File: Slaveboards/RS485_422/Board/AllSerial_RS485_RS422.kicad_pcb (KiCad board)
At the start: 2 copper layers, 67.4 x 44.8 mm, 18 parts, among them IC1 7402D, IC2 MAX485CSA, IC3 MAX485CSA, IC4 MAX485CSA, IC5 MAX485CSA, J1 PinHeader_2x05_P2.54mm_Horizo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, X1 ALLSERIALSLAVE, X2 AKL18X-10W

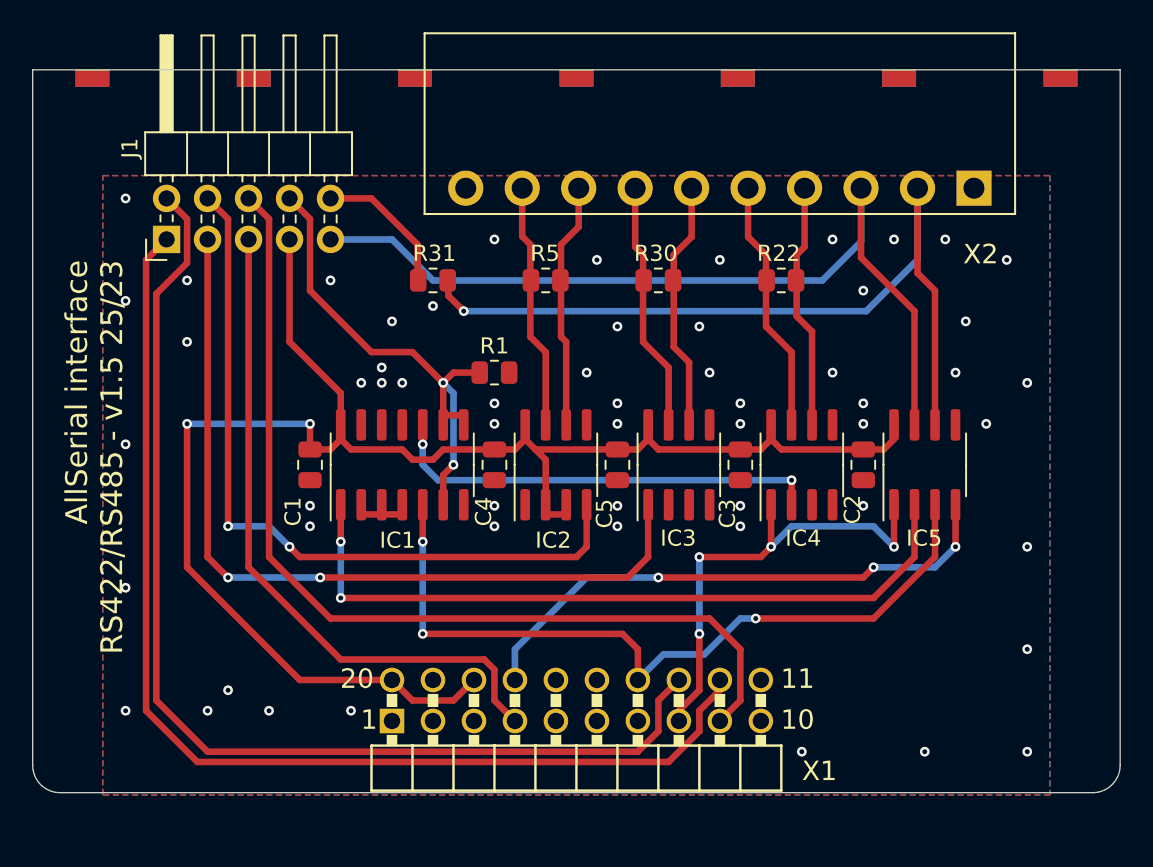
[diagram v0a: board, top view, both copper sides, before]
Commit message: Update AllSerial libraries
update projects
add slave project template
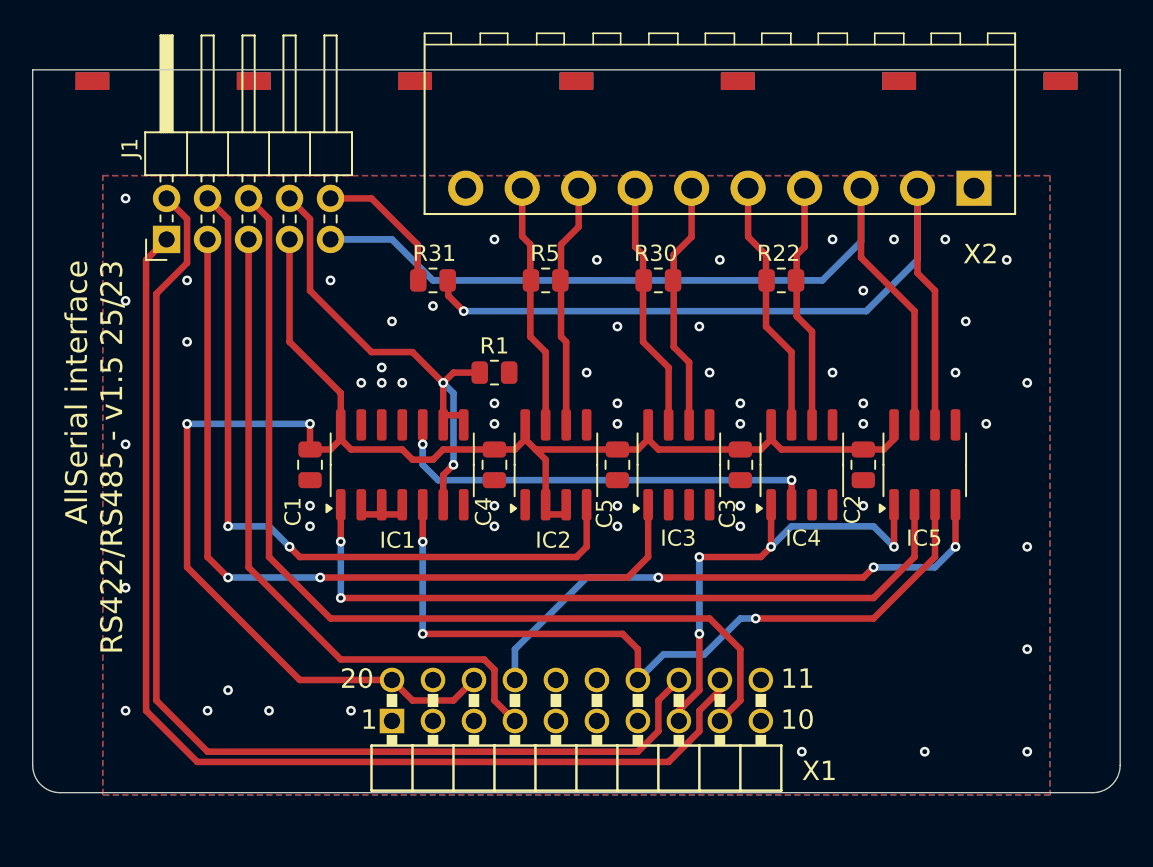
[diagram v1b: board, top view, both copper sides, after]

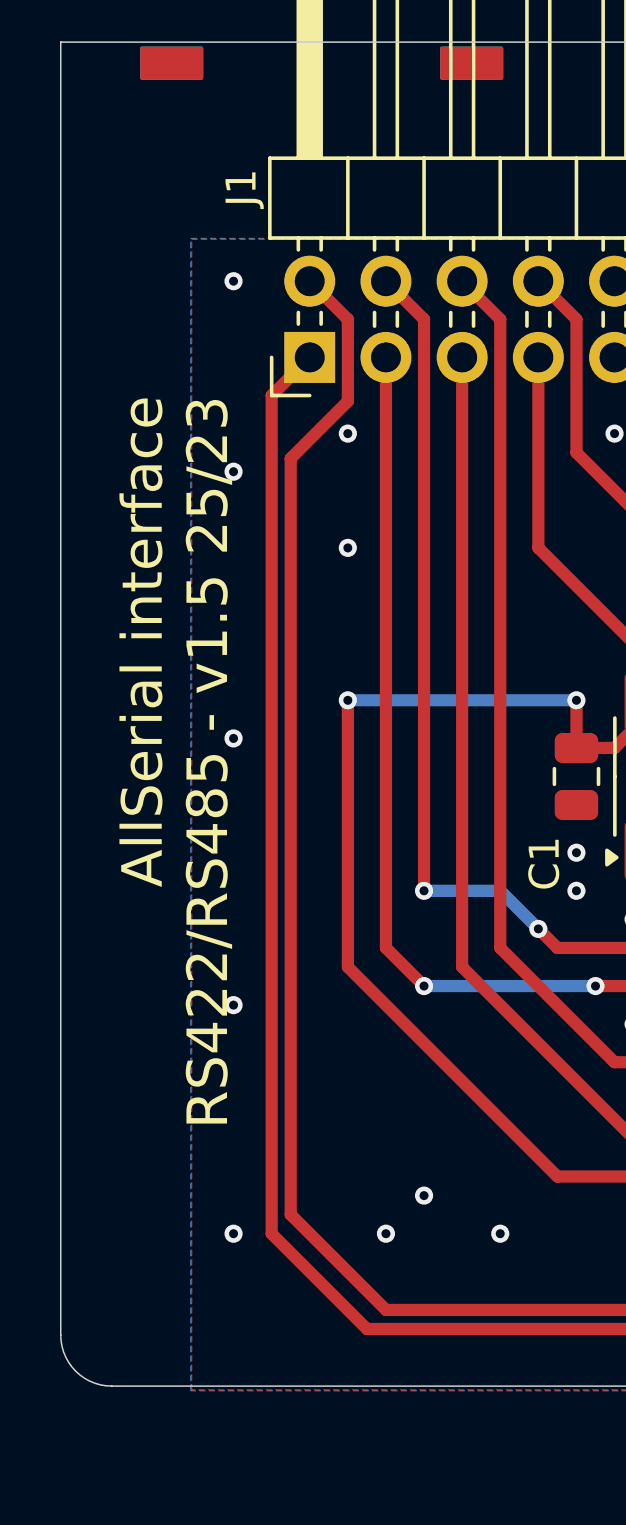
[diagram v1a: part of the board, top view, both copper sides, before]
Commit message: Migrate to KiCad 9
Add eBus board
Add various libraries
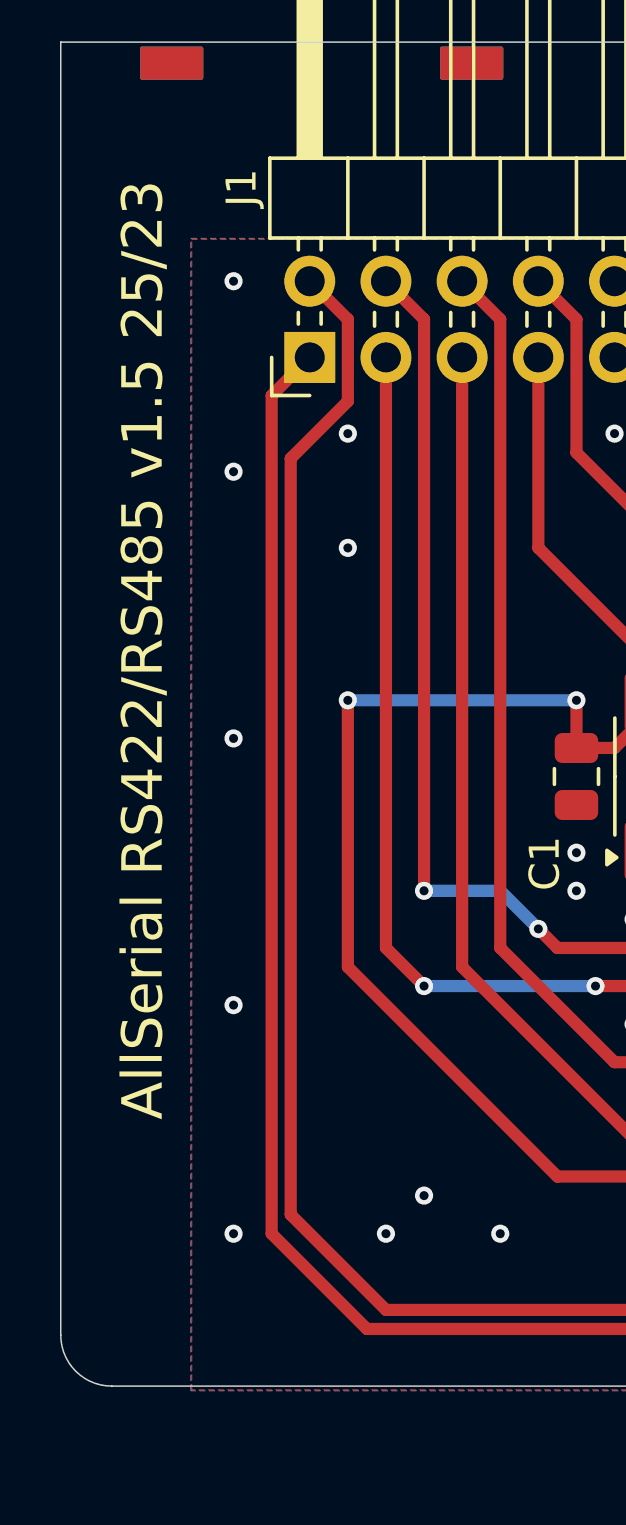
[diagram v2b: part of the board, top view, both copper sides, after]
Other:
- board text added: "AllSerial RS422/RS485 v1.5 25/23"
- board text removed: "AllSerial interface RS422/RS485 - v1.5 25/23"

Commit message: Improve libraries
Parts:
- added J2: Conn_02x03_Odd_Even, Connector_PinHeader_2.54mm:PinHeader_2x03_P2.54mm_Vertical, F.Cu at (151.4, 100.7)
- moved R5 3.45 mm to (149.5, 93.8), turned to 0 degrees
- moved R22 3.36 mm to (158.4, 93.8), turned to 0 degrees
- moved R30 2.03 mm to (154.4, 93.8)
- moved R31 1.85 mm to (139.6, 93.8)
- moved J1 1.19 mm to (123.1, 94.3)
- moved X2 0.46 mm to (157.4, 90.4)
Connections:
- R22 pad 1: Net-(IC4A-A) -> Net-(J2-Pin_6)
- R30 pad 2: Net-(IC3A-B) -> Net-(J2-Pin_4)
- R5 pad 2: Net-(IC2A-B) -> Net-(J2-Pin_2)
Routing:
- net Net-(IC4A-A): track 14.7 -> 21.1 mm, vias 0 -> 1
- net Net-(IC2A-B): track 14.7 -> 20.1 mm, vias 0 -> 1
- net Net-(J2-Pin_6): track 0.00 -> 4.84 mm
- net Net-(J2-Pin_2): track 0.00 -> 4.81 mm
- net Net-(J2-Pin_4): track 0.00 -> 4.59 mm
- net Net-(IC5A-A): track 50.7 -> 47.0 mm
- net /TERMB: track 53.7 -> 50.6 mm
- net /TERMA: track 8.80 -> 6.52 mm
- net /CTS_DSR: track 50.7 -> 48.9 mm
- net /RTS_DTR: track 46.1 -> 44.5 mm
- net /RXD: track 28.1 -> 26.6 mm
- net /RTS: track 59.3 -> 58.1 mm
- net /DTR: track 69.1 -> 67.9 mm
- net /RS422EN: track 31.3 -> 30.1 mm
- net /DSR: track 69.8 -> 68.6 mm
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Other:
- board text added: "AllSerial RS422/RS485 v1.6 27/25"
- board text added: "RX"
- board text added: "Term"
- board text added: "XI"
- board text added: "XO"
- board text removed: "AllSerial RS422/RS485 v1.5 25/23"

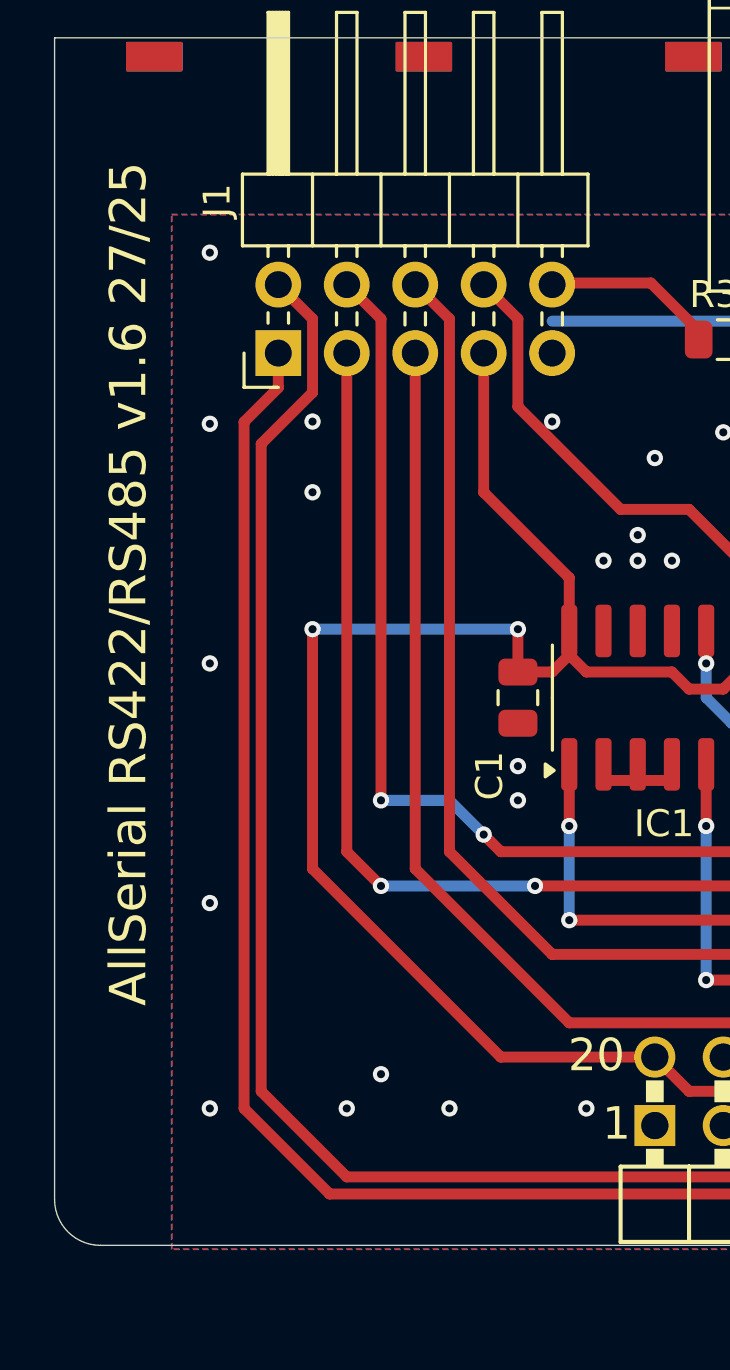
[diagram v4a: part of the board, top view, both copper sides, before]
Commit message: Add python testskript
Add mainboard tester
Add libraries
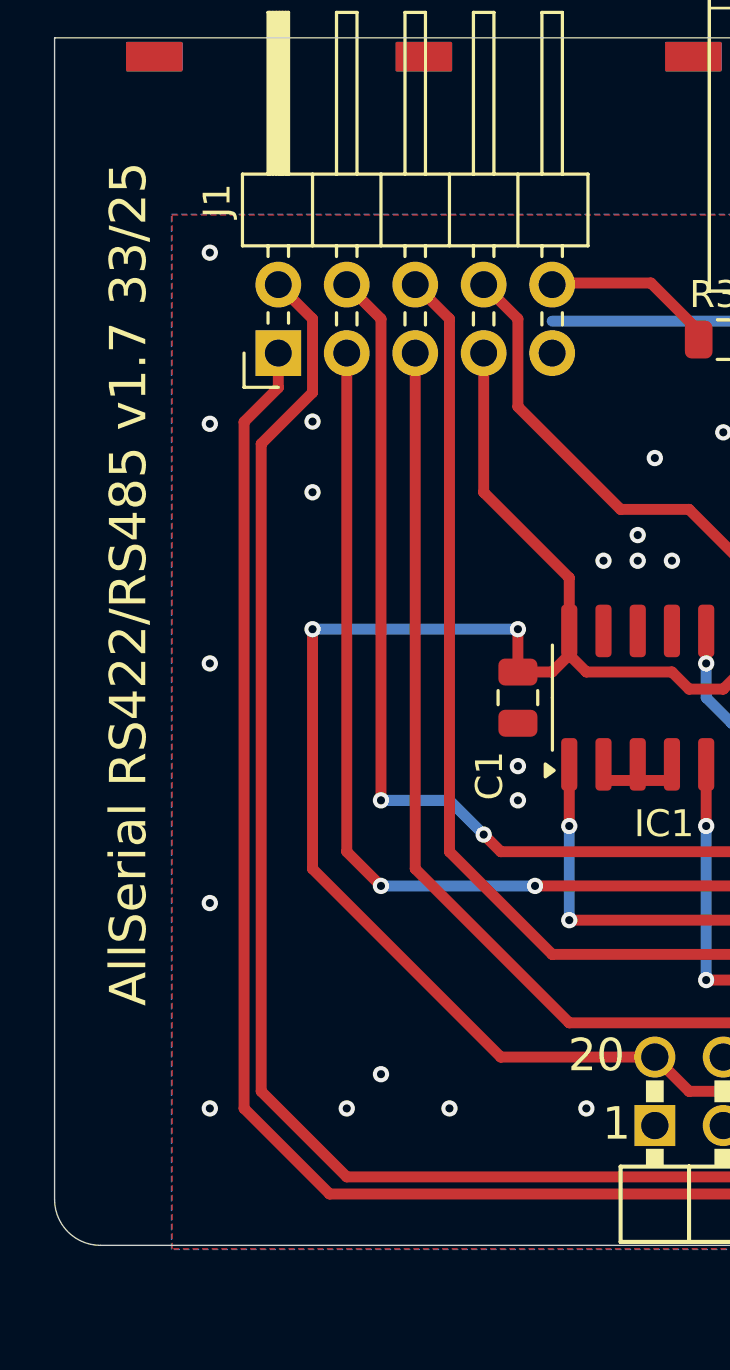
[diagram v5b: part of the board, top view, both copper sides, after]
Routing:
- net GND: vias 50 -> 49
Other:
- board text added: "AllSerial RS422/RS485 v1.7 33/25"
- board text removed: "AllSerial RS422/RS485 v1.6 27/25"
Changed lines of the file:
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@@
 		)
 	)
-	(gr_text "AllSerial RS422/RS485 v1.6 27/25"
+	(gr_text "AllSerial RS422/RS485 v1.7 33/25"
 		(at 116.7511 87.2 90)
 		(layer "F.SilkS")
@@
 		(size 0.6048)
 		(drill 0.3)
-		(layers "F.Cu" "B.Cu")
-		(net 1)
-	)
-	(via
-		(at 133.2611 96.84)
-		(size 0.6048)
-		(drill 0.3)
